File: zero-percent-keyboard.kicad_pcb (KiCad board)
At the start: 2 copper layers, 324.1 x 118.4 mm, 197 parts, among them J1 USB4085-GF-A_REVA, SW1 SW_PUSH, U1 ATMEGA32U4, X1 XTAL_GND

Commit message: Route traces
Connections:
- U1 pad 25: COL8 -> ROW5
- U1 pad 31: COL6 -> COL0
- U1 pad 32: COL5 -> COL1
- U1 pad 39: COL1 -> Net-(U1-Pad39)
- U1 pad 40: COL0 -> Net-(U1-Pad40)
- U1 pad 9: ROW5 -> Net-(U1-Pad9)
- X1 pad 2: GND -> XTAL2
- X1 pad 3: XTAL2 -> GND
- X1 pad 4: GND -> (no net)
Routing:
- net ROW0: track 338.3 -> 596.0 mm
- net ROW1: track 342.0 -> 578.4 mm
- net ROW2: track 336.7 -> 554.3 mm
- net +5V: track 13.5 -> 228.1 mm, vias 2 -> 8
- net ROW5: track 331.6 -> 524.1 mm

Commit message: Progress
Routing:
- net ROW3: track 332.9 -> 535.2 mm

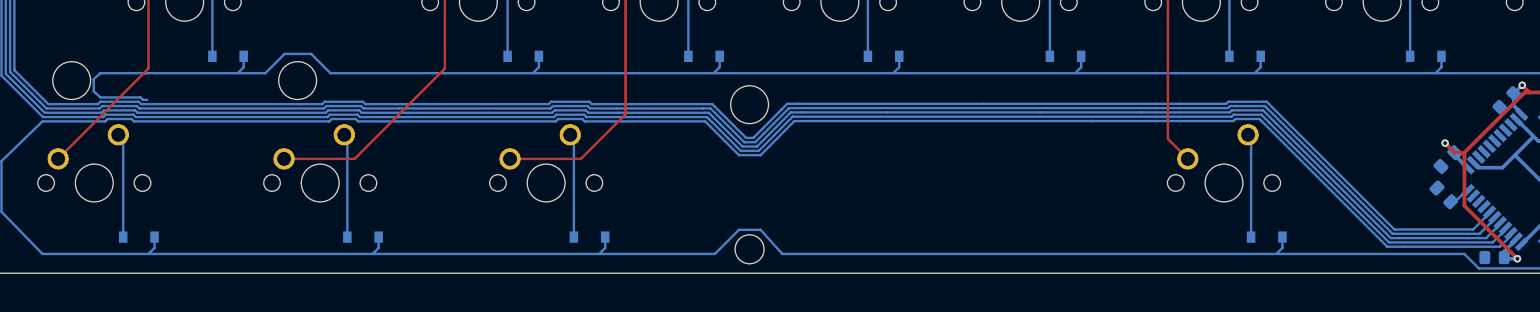
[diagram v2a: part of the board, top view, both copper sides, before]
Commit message: Rearrange rows and columns in schematic
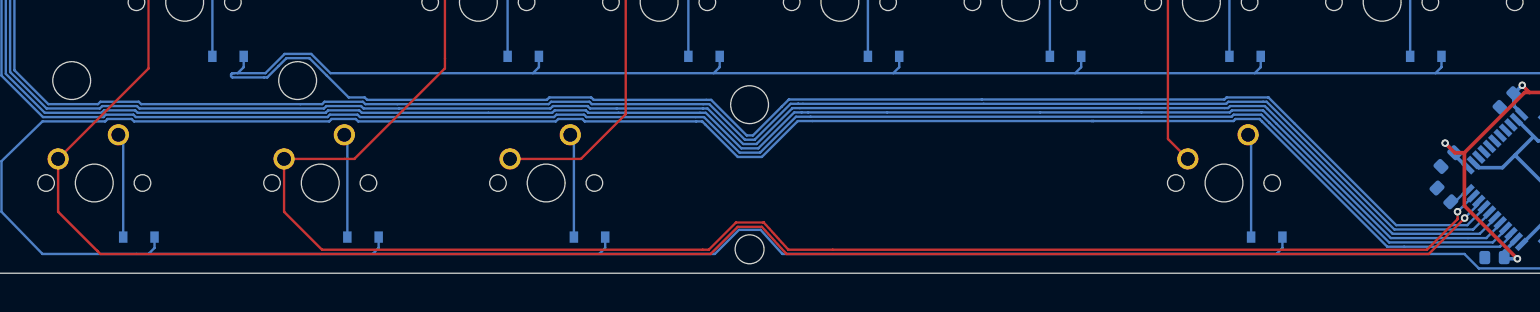
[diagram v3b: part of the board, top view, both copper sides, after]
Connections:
- U1 pad 10: COL15 -> COL10
- U1 pad 11: COL14 -> COL11
- U1 pad 12: COL13 -> Net-(U1-Pad12)
- U1 pad 18: COL13 -> COL12
- U1 pad 19: COL12 -> COL13
- U1 pad 20: COL11 -> COL14
- U1 pad 21: COL10 -> COL15
- U1 pad 22: COL9 -> Net-(U1-Pad22)
- U1 pad 36: COL4 -> COL2
- U1 pad 38: COL2 -> COL4
- U1 pad 39: Net-(U1-Pad39) -> COL5
- U1 pad 40: Net-(U1-Pad40) -> COL6
- U1 pad 8: Net-(U1-Pad8) -> COL8
- U1 pad 9: Net-(U1-Pad9) -> COL9
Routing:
- net COL0: track 104.3 -> 265.9 mm, vias 0 -> 1
- net COL1: track 118.3 -> 256.0 mm, vias 0 -> 1
- net ROW4: track 348.7 -> 471.0 mm

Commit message: Progress
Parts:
- moved SW1 60.6 mm to (201.2, 156.9)
- moved R6 60.6 mm to (208.1, 159.1)
- moved D12 22.3 mm to (275.1, 46.9)
- moved D60 22.3 mm to (275.1, 104.0)
- moved MX85 22.3 mm to (275.2, 136.4)
- moved D28 22.3 mm to (260.9, 65.9)
- moved MX12 22.3 mm to (270.5, 41.2)
- moved MX29 22.3 mm to (275.2, 60.2)
- moved MX44 22.3 mm to (265.7, 79.3)
- moved MX60 22.3 mm to (270.5, 98.3)
- moved D22 22.3 mm to (146.4, 65.9)
- moved MX68 22.3 mm to (146.7, 117.4)
- moved C3 22.3 mm to (191.7, 133.9)
- moved C6 22.3 mm to (202.9, 127.2)
- moved D10 22.3 mm to (237.0, 46.9)
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
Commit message: Finished PCB
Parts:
- moved SW1 32.2 mm to (225.6, 135.9), turned to 90 degrees
- moved R6 26.6 mm to (221.0, 135.9), turned to 270 degrees
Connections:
- X1 pad 2: XTAL2 -> GND
- X1 pad 3: GND -> XTAL2
- X1 pad 4: (no net) -> GND
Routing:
- net COL15: track 95.2 -> 252.5 mm, vias 0 -> 1
- net COL14: track 95.2 -> 232.8 mm, vias 0 -> 1
- net COL2: track 115.6 -> 239.5 mm, vias 0 -> 1
- net COL13: track 106.9 -> 224.2 mm, vias 0 -> 1
- net COL3: track 87.3 -> 197.1 mm, vias 0 -> 1
- net COL12: track 112.6 -> 210.0 mm, vias 0 -> 1
- net COL4: track 87.3 -> 178.6 mm, vias 0 -> 1
- net GND: track 38.8 -> 115.5 mm, vias 0 -> 20
- net COL11: track 112.0 -> 187.0 mm, vias 0 -> 1
- net (no net): track 0.00 -> 66.3 mm
- net COL10: track 116.1 -> 173.1 mm, vias 0 -> 1
- net COL6: track 89.7 -> 144.1 mm, vias 0 -> 1
- net COL5: track 109.0 -> 160.4 mm, vias 0 -> 1
- net COL9: track 116.3 -> 154.8 mm, vias 0 -> 1
- net COL8: track 89.4 -> 114.2 mm, vias 0 -> 1
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- added copper zone on B.Cu, net GND
- added copper zone on F.Cu, net GND
